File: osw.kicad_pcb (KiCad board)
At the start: 4 copper layers, 45 x 41 mm, 70 parts, among them J1 Conn_01x02, Q1 2N7002, SW1 SW_Push, SW2 SW_Push, SW4 SW_Push, SW5 SW_Push, U1 DS3231MZ, U10 XC6209, U11 MCP73831T-2ACI_OT, U13 XC6209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

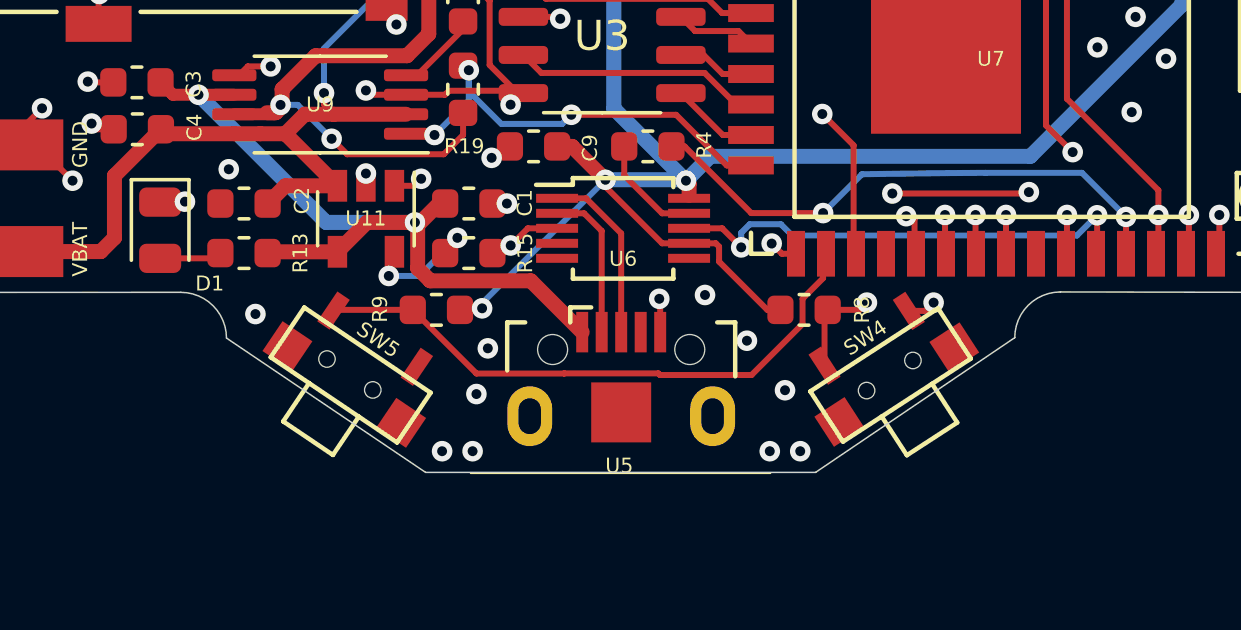
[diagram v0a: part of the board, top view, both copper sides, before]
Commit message: Moving this to kicad 6 and looking at potential solutions to adding a buzzer and heart-rate monitor.  Have to see if original repo owner is open to this.
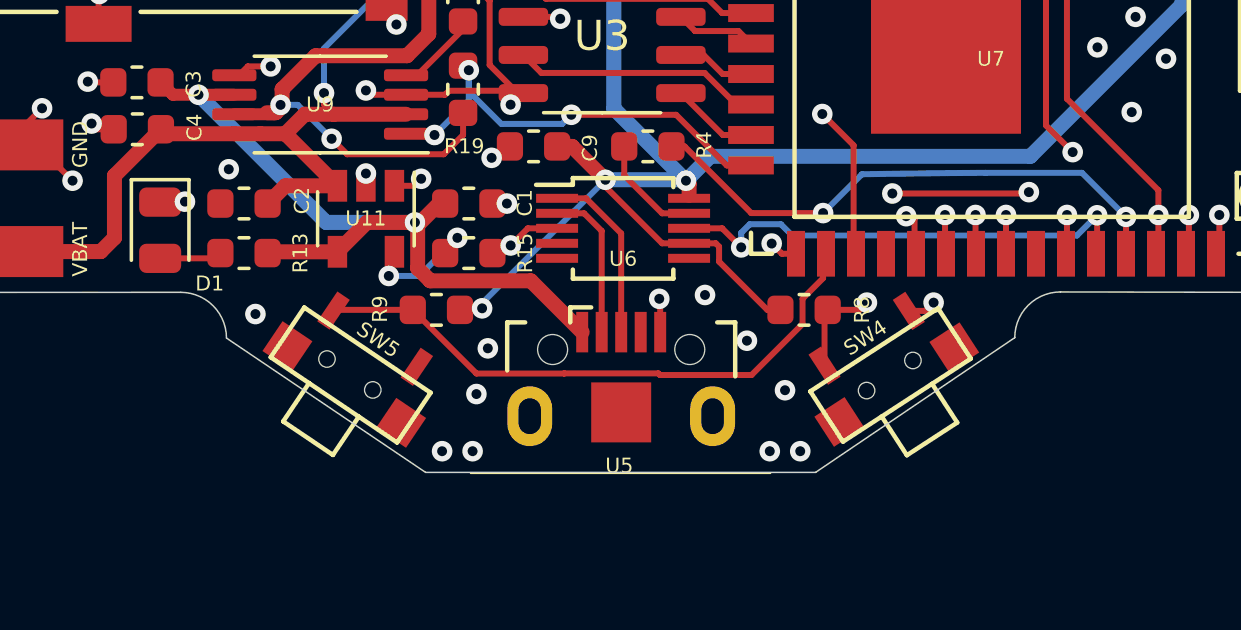
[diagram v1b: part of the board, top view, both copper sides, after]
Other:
- net class Default removed

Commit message: Updating the libs to kicad 6 as well.
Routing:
- net GND: track 86.4 -> 77.5 mm, vias 75 -> 69
- net /3V3_2: track 56.4 -> 59.1 mm, vias 2 -> 4
- net /TFT_CS: track 32.8 -> 34.6 mm, vias 2 -> 3
- net /TFT_DC: track 33.4 -> 35.2 mm, vias 2 -> 3
- net Net-(U8-Pad23): track 0.00 -> 1.35 mm, vias 0 -> 1
- net Net-(U8-Pad6): track 0.00 -> 1.30 mm, vias 0 -> 1

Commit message: Updates to the board and schematic.
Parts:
- removed R10, R9: 10k, Resistor_SMD:R_0603_1608Metric
- removed SW1, SW2, SW4, SW5: SW_Push, open-Smartwatch:button_side_smd
- R8: value 10k -> res0402_10k; footprint Resistor_SMD:R_0603_1608Metric -> open-Smartwatch:R_0402_1005Metric_osw
- moved R8 30.7 mm to (151.5, 98.0)
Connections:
- R8 pad 1: +3V3 -> /BTN2
- R8 pad 2: /EN -> GND
- U1 pad 1: Net-(U1-Pad1) -> unconnected-(U1-Pad1)
- U1 pad 4: Net-(U1-Pad4) -> unconnected-(U1-Pad4)
- U10 pad 4: Net-(U10-Pad4) -> unconnected-(U10-Pad4)
- U13 pad 4: Net-(U13-Pad4) -> unconnected-(U13-Pad4)
- U2 pad 11: Net-(U2-Pad11) -> unconnected-(U2-Pad11)
- U2 pad 4: Net-(U2-Pad4) -> unconnected-(U2-Pad4)
- U5 pad 2: Net-(U5-Pad2) -> unconnected-(U5-Pad2)
- U5 pad 6: (no net) -> unconnected-(U5-Pad6)
- U6 pad 4: Net-(U6-Pad4) -> unconnected-(U6-Pad4)
- U6 pad 5: Net-(U6-Pad5) -> unconnected-(U6-Pad5)
- U6 pad 6: Net-(U6-Pad6) -> unconnected-(U6-Pad6)
- U7 pad 27: Net-(U7-Pad27) -> unconnected-(U7-Pad27)
- U7 pad 32: Net-(U7-Pad32) -> unconnected-(U7-Pad32)
- U8 pad 1: Net-(U8-Pad1) -> unconnected-(U8-Pad1)
- U8 pad 20: Net-(U8-Pad20) -> unconnected-(U8-Pad20)
- U8 pad 23: Net-(U8-Pad23) -> unconnected-(U8-Pad23)
- U8 pad 29: Net-(U8-Pad29) -> unconnected-(U8-Pad29)
- U8 pad 3: Net-(U8-Pad3) -> unconnected-(U8-Pad3)
- U8 pad 30: Net-(U8-Pad30) -> unconnected-(U8-Pad30)
- U8 pad 6: Net-(U8-Pad6) -> unconnected-(U8-Pad6)
- U8 pad 7: Net-(U8-Pad7) -> unconnected-(U8-Pad7)
- XS1 pad 1: Net-(XS1-Pad1) -> unconnected-(XS1-Pad1)
- XS1 pad 8: Net-(XS1-Pad8) -> unconnected-(XS1-Pad8)
- XS1 pad 9: Net-(XS1-Pad9) -> unconnected-(XS1-Pad9)
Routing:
- net /TFT_DC: track 35.2 -> 1.79 mm, vias 3 -> 1
- net GND: track 77.5 -> 109.7 mm, vias 69 -> 71
- net Net-(R1-Pad2): track 16.0 -> 0.00 mm, vias 2 -> 0
- net /MOSI: track 41.1 -> 57.1 mm, vias 5 -> 7
- net /LEDK: track 15.3 -> 0.00 mm, vias 2 -> 0
- net /TFT_RST: track 21.1 -> 36.4 mm, vias 2 -> 4
- net unconnected-(U8-Pad23): track 0.00 -> 1.35 mm, vias 0 -> 1
- net Net-(U8-Pad23): track 1.35 -> 0.00 mm, vias 1 -> 0
- net unconnected-(U8-Pad6): track 0.00 -> 1.30 mm, vias 0 -> 1
- net Net-(U8-Pad6): track 1.30 -> 0.00 mm, vias 1 -> 0
- net Net-(R5-Pad1): track 2.43 -> 3.59 mm

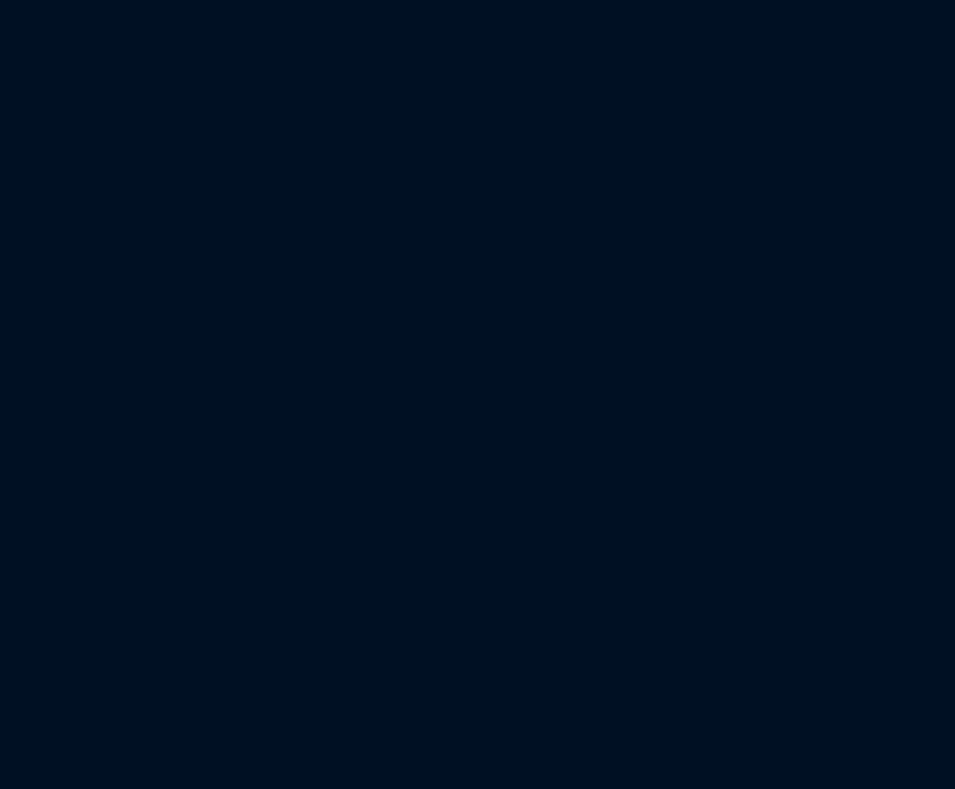
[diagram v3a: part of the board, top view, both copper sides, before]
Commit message: Adding a very small regulater for running everything.
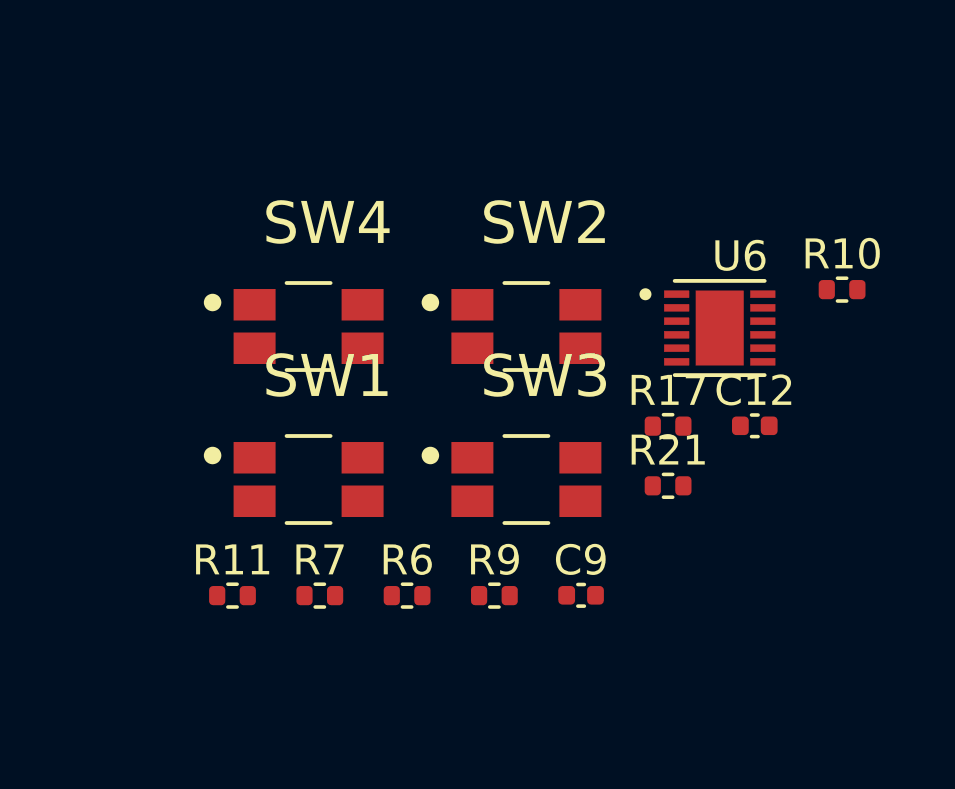
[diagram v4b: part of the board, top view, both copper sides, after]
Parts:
- added C12: 1u, open-Smartwatch:C_0402_1005Metric_osw, F.Cu at (209.8, 101.3)
- added C9: cap0402_p1u10V, open-Smartwatch:C_0402_1005Metric_osw, F.Cu at (204.0, 107.0)
- added R10: res0402_10k, open-Smartwatch:R_0402_1005Metric_osw, F.Cu at (212.7, 96.8)
- added R11: res0402_10k, open-Smartwatch:R_0402_1005Metric_osw, F.Cu at (192.4, 107.0)
- added R17: res0402_10k, open-Smartwatch:R_0402_1005Metric_osw, F.Cu at (206.9, 101.4)
- added R21: res0402_10k, open-Smartwatch:R_0402_1005Metric_osw, F.Cu at (206.9, 103.3)
- added R6: res0402_10k, open-Smartwatch:R_0402_1005Metric_osw, F.Cu at (198.2, 107.0)
- added R7: res0402_10k, open-Smartwatch:R_0402_1005Metric_osw, F.Cu at (195.3, 107.0)
- added R9: res0402_10k, open-Smartwatch:R_0402_1005Metric_osw, F.Cu at (201.1, 107.0)
- added SW1: SPST_EVQ-P7J01P, open-Smartwatch:SW_EVQ-P7J01P, F.Cu at (194.9, 103.1)
- added SW2: SPST_EVQ-P7J01P, open-Smartwatch:SW_EVQ-P7J01P, F.Cu at (202.2, 98.0)
- added SW3: SPST_EVQ-P7J01P, open-Smartwatch:SW_EVQ-P7J01P, F.Cu at (202.2, 103.1)
- added SW4: SPST_EVQ-P7J01P, open-Smartwatch:SW_EVQ-P7J01P, F.Cu at (194.9, 98.0)
- added U6: FT234XD-R, open-Smartwatch:SON45P300X300X80-13N, F.Cu at (208.6, 98.1)
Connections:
- Q1 pad 3: /LEDK -> unconnected-(Q1-Pad3)
- R4 pad 1: Net-(R4-Pad1) -> unconnected-(R4-Pad1)
- U3 pad 1: /GPIO10 -> unconnected-(U3-Pad1)
- U3 pad 2: /SD0 -> unconnected-(U3-Pad2)
- U3 pad 3: /SD3 -> unconnected-(U3-Pad3)
- U3 pad 4: GND -> unconnected-(U3-Pad4)
- U3 pad 5: /SD1 -> unconnected-(U3-Pad5)
- U3 pad 6: /CLK -> unconnected-(U3-Pad6)
- U3 pad 7: /SD2 -> unconnected-(U3-Pad7)
- U3 pad 8: +3V3 -> unconnected-(U3-Pad8)
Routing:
- net unconnected-(U8-Pad3): track 0.00 -> 24.3 mm, vias 0 -> 2
- net /GEO_F2V8: track 24.3 -> 0.00 mm, vias 2 -> 0
- net /GPS_TX2V8: track 17.2 -> 36.3 mm, vias 2 -> 4
- net /3DFIX_2V8: track 19.1 -> 0.00 mm, vias 2 -> 0
- net unconnected-(U3-Pad1): track 0.00 -> 8.06 mm
- net /GPIO10: track 8.06 -> 0.00 mm
- net unconnected-(U3-Pad7): track 0.00 -> 2.71 mm
- net /SD2: track 2.71 -> 0.00 mm
- net GND: track 109.7 -> 107.3 mm, vias 71 -> 70
- net Net-(R5-Pad1): track 3.59 -> 6.02 mm, vias 1 -> 2

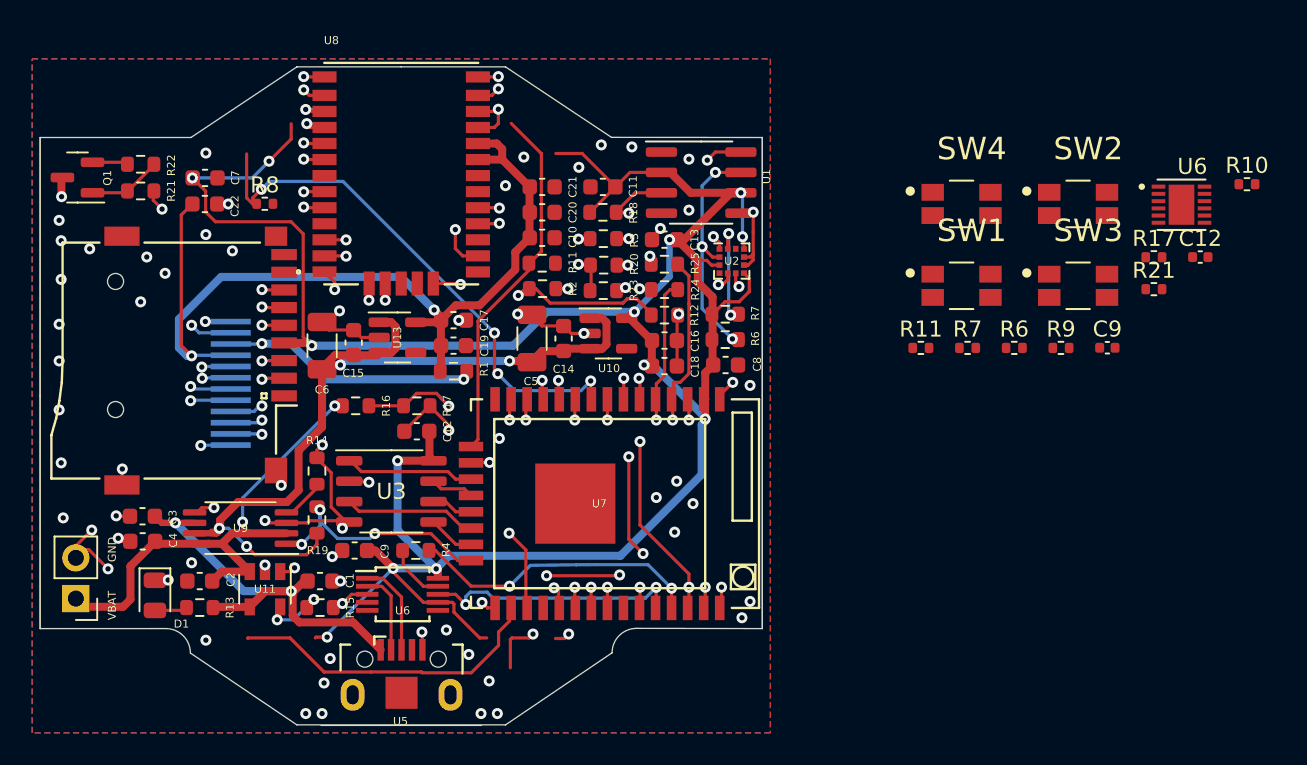
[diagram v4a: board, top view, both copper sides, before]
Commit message: Updating the display connector footprint.
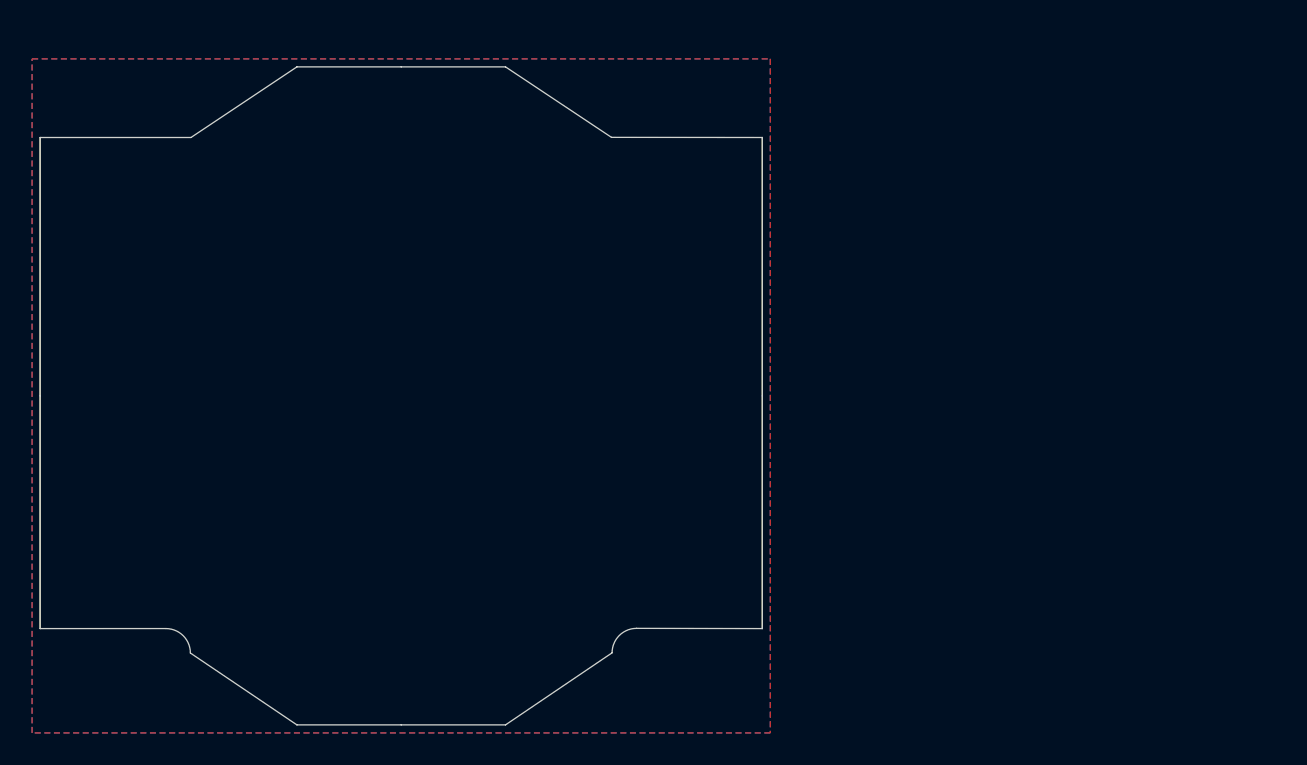
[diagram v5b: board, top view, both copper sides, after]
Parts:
- removed C1, C2: 4.7uF, Capacitor_SMD:C_0603_1608Metric
- removed C10, C11, C12, C13, C14, C15, C18, C19, C22, C3, C4, C7, C8, C9: 0.1u, Capacitor_SMD:C_0603_1608Metric
- removed C12: 1u, open-Smartwatch:C_0402_1005Metric_osw
- removed C16, C17: 4.7u, Capacitor_SMD:C_0603_1608Metric
- removed C20: 100p, Capacitor_SMD:C_0603_1608Metric
- removed C21: 10p, Capacitor_SMD:C_0603_1608Metric
- removed C5, C6: 100u, Capacitor_SMD:C_1206_3216Metric
- removed C9: cap0402_p1u10V, open-Smartwatch:C_0402_1005Metric_osw
- removed D1: LED_Green, LED_SMD:LED_0805_2012Metric
- removed G***: LOGO, footprints:p3dt_tiny
- removed G***: LOGO, footprints:aisler_15x12mm
- removed J1: Conn_01x02, Connector_PinHeader_2.54mm:PinHeader_1x02_P2.54mm_Vertical
- removed Q1: 2N7002, Package_TO_SOT_SMD:SOT-23
- removed R1: 22, Resistor_SMD:R_0603_1608Metric
- removed R10, R11, R17, R21, R6, R7, R8, R9: res0402_10k, open-Smartwatch:R_0402_1005Metric_osw
- removed R11, R17, R20, R21: 10k, Resistor_SMD:R_0603_1608Metric
- removed R12: 5.6k, Resistor_SMD:R_0603_1608Metric
- removed R13, R4: 470R, Resistor_SMD:R_0603_1608Metric
- removed R14: 510R, Resistor_SMD:R_0603_1608Metric
- removed R15: 5k, Resistor_SMD:R_0603_1608Metric
- removed R16, R19: 200k, Resistor_SMD:R_0603_1608Metric
- removed R18: 2.2K, Resistor_SMD:R_0603_1608Metric
- removed R2, R24, R25, R3, R6, R7: 1k, Resistor_SMD:R_0603_1608Metric
- removed R22: 1M, Resistor_SMD:R_0603_1608Metric
- removed R23: 56k, Resistor_SMD:R_0603_1608Metric
- removed R5: 0R, Resistor_SMD:R_0402_1005Metric
- removed REF**: KiCad-Logo2_5mm_SilkScreen, Symbol:KiCad-Logo2_5mm_SilkScreen
- removed SW1, SW2, SW3, SW4: SPST_EVQ-P7J01P, open-Smartwatch:SW_EVQ-P7J01P
- removed U1: DS3231MZ, Package_SO:SOIC-8_3.9x4.9mm_P1.27mm
- removed U10, U13: XC6209, Package_TO_SOT_SMD:SOT-23-5
- removed U11: MCP73831T-2ACI_OT, open-Smartwatch:SOT-23-5
- removed U2: BMA400, open-Smartwatch:LGA-12_2x2mm_P0.5mm
- removed U3: PSRAM64H, Package_SO:SOP-8_3.9x4.9mm_P1.27mm
- removed U4: GC9A01_IPS_display, open-Smartwatch:GC9A01_IPS_display
- removed U5: USB-OTG, open-Smartwatch:USBmicro-B
- removed U6: CH340E, open-Smartwatch:MSOP-10_3x3mm_P0.5mm
- removed U6: FT234XD-R, open-Smartwatch:SON45P300X300X80-13N
- removed U7: ttgo-32-micro, open-Smartwatch:ttgo-32-micro
- removed U8: Quectel_L96, open-Smartwatch:Quectel_L96
- removed U9: TPS2115A, open-Smartwatch:TSSOP-8_4.4x3mm_P0.65mm
- removed XS1: SD_ebay-uSD-push_push_SMD, open-Smartwatch:Conn_uSDcard
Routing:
- net +3V3: track 160.1 -> 0.00 mm, vias 13 -> 0
- net GND: track 107.3 -> 0.00 mm, vias 70 -> 0
- net /3V3_2: track 59.1 -> 0.00 mm, vias 4 -> 0
- net /MOSI: track 57.1 -> 0.00 mm, vias 7 -> 0
- net /VCC: track 52.6 -> 0.00 mm, vias 4 -> 0
- net /SCK: track 38.5 -> 0.00 mm, vias 3 -> 0
- net /TFT_RST: track 36.4 -> 0.00 mm, vias 4 -> 0
- net /GPS_TX2V8: track 36.3 -> 0.00 mm, vias 4 -> 0
- net /SCL: track 36.1 -> 0.00 mm, vias 5 -> 0
- net /SDA: track 35.0 -> 0.00 mm, vias 6 -> 0
- net /TFT_CS: track 34.6 -> 0.00 mm, vias 3 -> 0
- net /BTN2: track 33.3 -> 0.00 mm, vias 4 -> 0
- net /MISO: track 32.8 -> 0.00 mm, vias 2 -> 0
- net /VBAT: track 32.4 -> 0.00 mm, vias 2 -> 0
- net /PIN_LED: track 29.5 -> 0.00 mm, vias 2 -> 0
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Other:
- board text removed: "1"
- board text removed: "2"
- board text removed: "3"
- board text removed: "@pauls_3d_things"
- board text removed: "GND"
- board text removed: "R"
- board text removed: "V 3.1"
- board text removed: "VBAT"
- board text removed: "open-smartwatch.github.io"
